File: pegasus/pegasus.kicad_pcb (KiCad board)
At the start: 2 copper layers, 50 x 120 mm, 17 parts, among them IC1 L7805ACV, IC2 RFD900, IC3 L70B-M39, J1 Screw_Terminal_01x02, U1 Teensy4.0, U2 CON-SMA-EDGE-S, U3 CON-SMA-EDGE-S

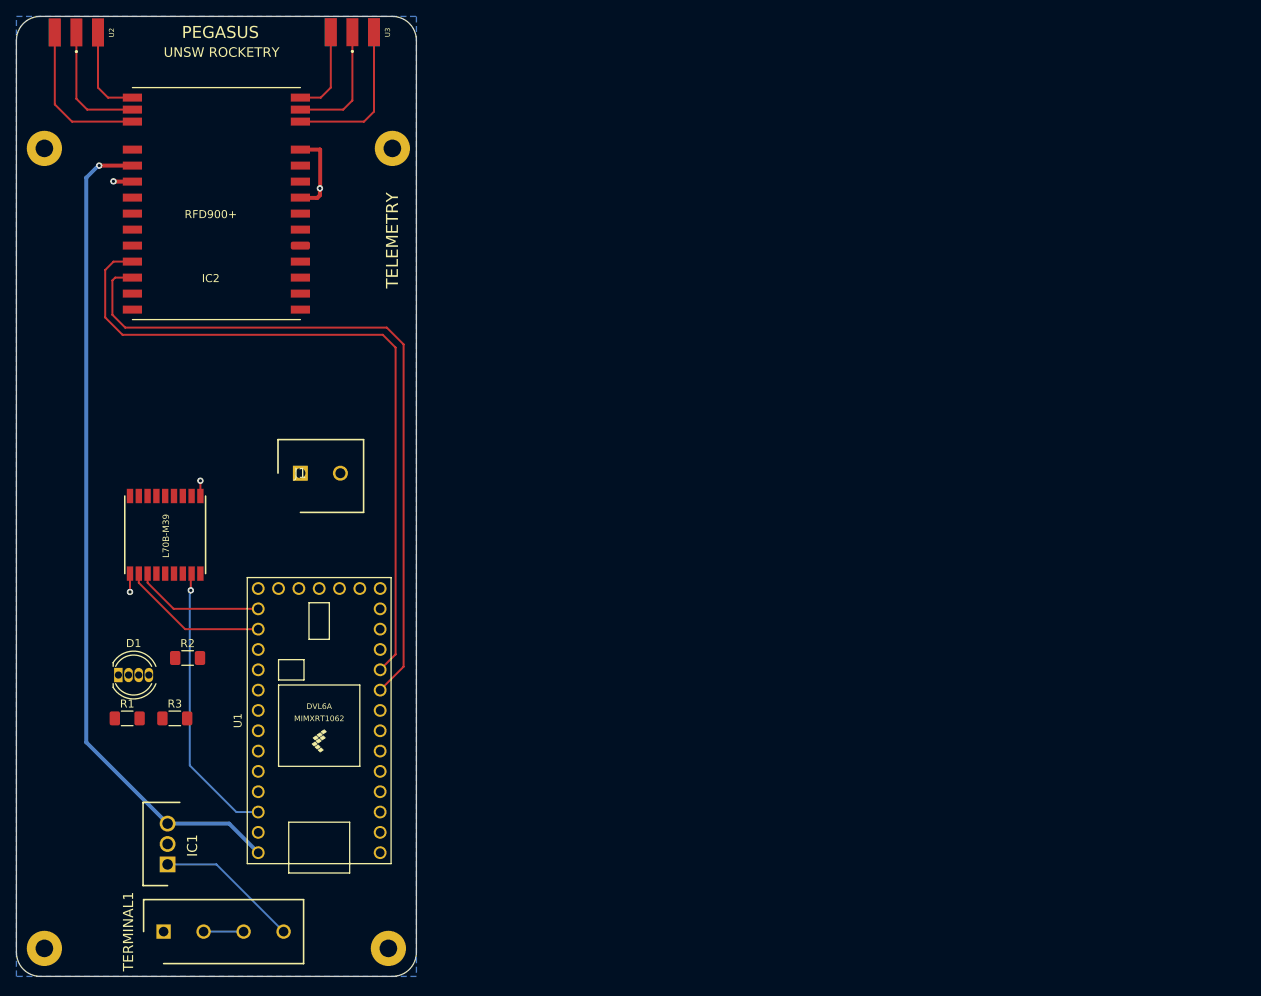
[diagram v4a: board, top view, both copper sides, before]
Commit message: change mount holes to m3, draft new component layout, reduce size  to 39x105mm
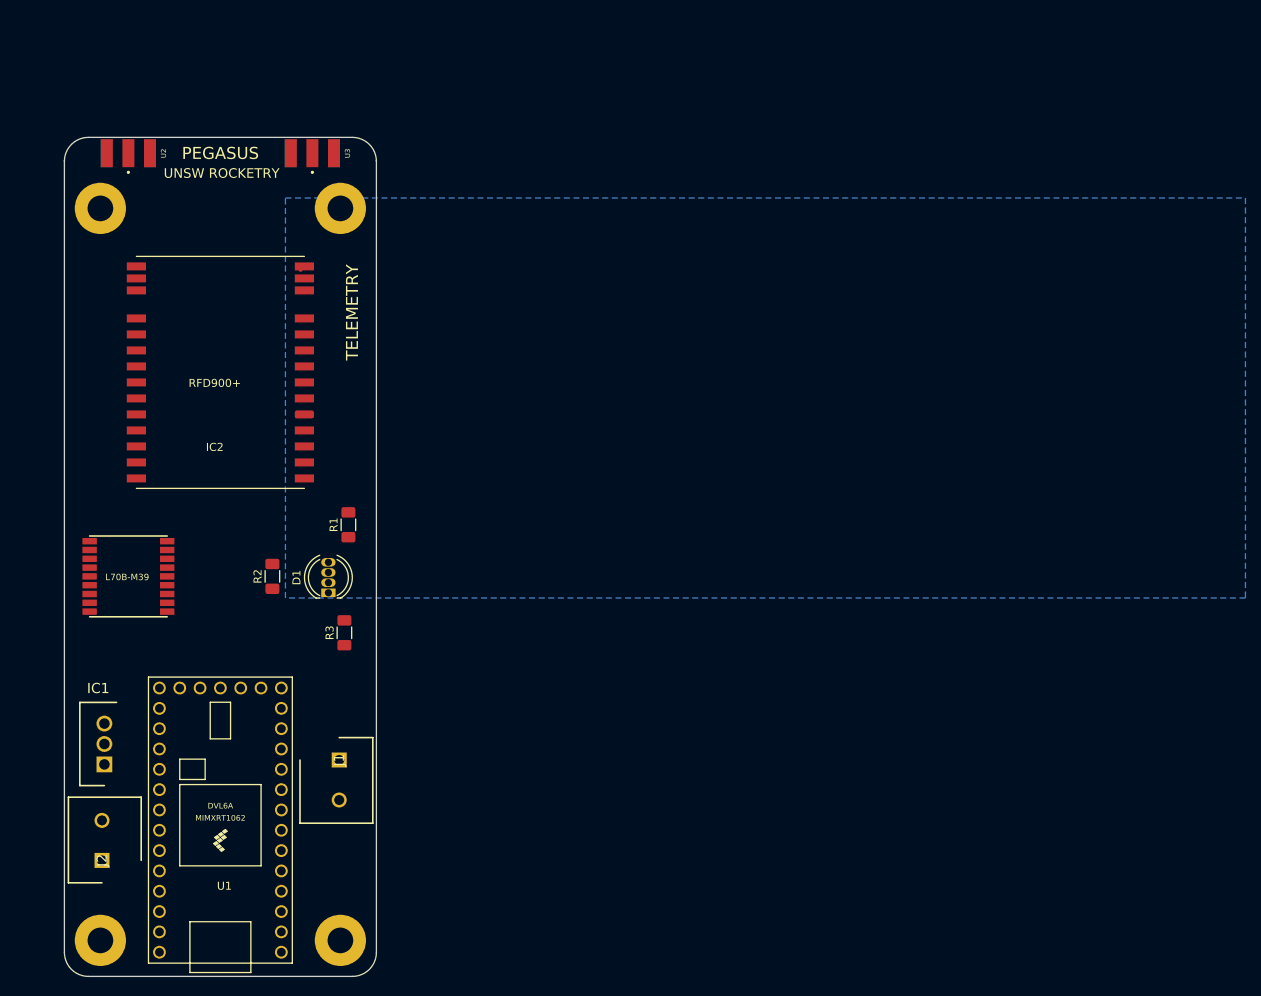
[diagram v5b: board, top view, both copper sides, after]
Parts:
- removed TERMINAL1: Screw_Terminal_01x04, RS-Components:SHDR4W100P0X500_1X4_2000X800X1000P
- added J2: Screw_Terminal_01x02, RS-Components:SHDR2W105P0X500_1X2_1060X900X1250P, F.Cu at (90.7, 145.5)
- H1, H2, H3, H4: footprint MountingHole:MountingHole_2.2mm_M2_Pad -> MountingHole:MountingHole_3.2mm_M3_Pad
- moved R1 36.7 mm to (121.5, 103.5), turned to 90 degrees
- moved J1 36.2 mm to (120.3, 132.9), turned to -90 degrees
- moved D1 28.2 mm to (119.0, 112.0), turned to 90 degrees
- moved G*** 26.5 mm to (105.0, 85.0)
- moved R3 23.7 mm to (121.0, 117.0), turned to 90 degrees
- moved IC2 21.1 mm to (110.0, 87.8)
- moved U1 17.5 mm to (105.5, 140.5)
- moved U2 16.4 mm to (94.0, 57.1)
- moved U3 15.9 mm to (117.0, 57.1)
- moved IC1 14.8 mm to (91.0, 133.5)
- moved R2 14.7 mm to (112.0, 110.0), turned to 90 degrees
- moved H4 10.3 mm to (90.5, 64.0)
- moved H3 9.92 mm to (120.5, 64.0)
- moved H1 7.07 mm to (90.5, 155.5)
- moved IC3 6.94 mm to (94.0, 110.0), turned to 0 degrees
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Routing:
- net +5V: track 104.1 -> 0.00 mm, vias 1 -> 0
- net RX7: track 89.3 -> 0.00 mm
- net TX7: track 88.7 -> 0.00 mm
- net 3.3V: track 35.0 -> 0.00 mm, vias 1 -> 0
- net Net-(IC2-Pad12): track 19.6 -> 0.00 mm
- net Net-(IC2-Pad17): track 19.6 -> 0.00 mm
- net RX3: track 18.5 -> 0.00 mm
- net /BATT+: track 18.0 -> 0.00 mm
- net GND: track 17.4 -> 0.00 mm, vias 4 -> 0
- net TX3: track 16.3 -> 0.00 mm
- net Net-(IC2-Pad16): track 15.9 -> 0.00 mm
- net Net-(IC2-Pad13): track 15.5 -> 0.00 mm
- net Net-(IC2-Pad15): track 11.7 -> 0.00 mm
- net Net-(IC2-Pad14): track 11.2 -> 0.06 mm
- net Net-(TERMINAL1-Pad2): track 5.00 -> 0.00 mm
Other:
- board size 50 x 120 mm -> 39 x 104.9 mm

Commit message: add second rx-tx screw terminal connector, optimize pin assignment for other components
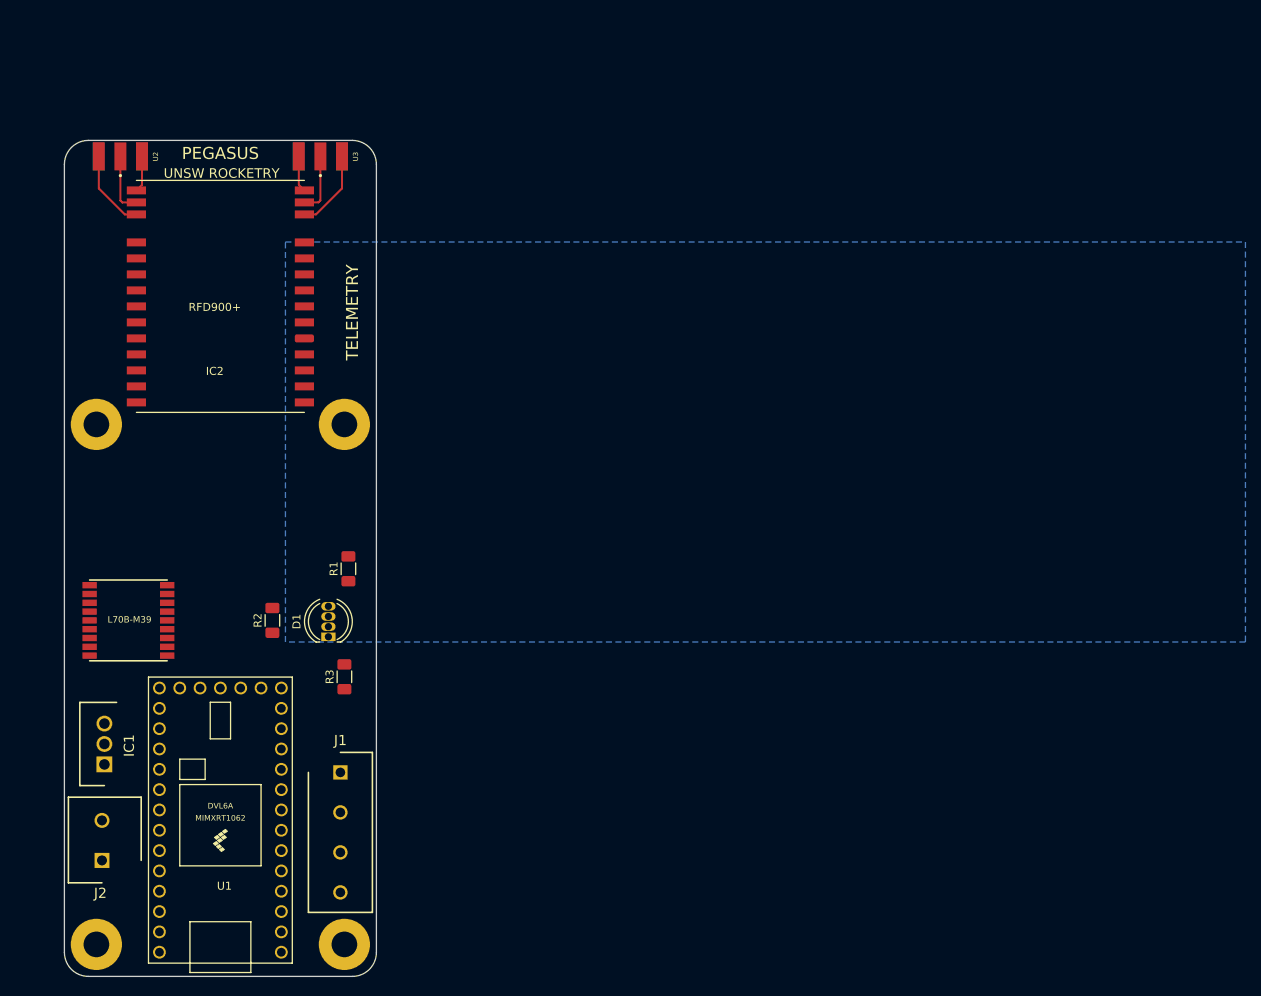
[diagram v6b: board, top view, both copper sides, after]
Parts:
- J1: value Screw_Terminal_01x02 -> Screw_Terminal_01x04; footprint RS-Components:SHDR2W105P0X500_1X2_1060X900X1250P -> RS-Components:SHDR4W100P0X500_1X4_2000X800X1000P
- moved H3 27.0 mm to (121.0, 91.0)
- moved H4 27.0 mm to (90.0, 91.0)
- moved IC2 9.50 mm to (110.0, 78.2)
- moved D1 5.50 mm to (119.0, 117.5)
- moved IC3 5.50 mm to (94.0, 115.5), turned to 180 degrees
- moved R1 5.50 mm to (121.5, 109.0)
- moved R2 5.50 mm to (112.0, 115.5)
- moved R3 5.50 mm to (121.0, 122.5)
- moved J1 1.56 mm to (120.5, 134.5)
- moved U2 1.08 mm to (93.0, 57.5)
- moved U3 1.08 mm to (118.0, 57.5)
- moved H1 0.71 mm to (90.0, 156.0)
- moved H2 0.71 mm to (121.0, 156.0)
- moved G*** 0.50 mm to (105.5, 85.0)
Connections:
- IC2 pad 25: TX7 -> TX3
- IC2 pad 26: RX7 -> RX3
- IC3 pad 2: RX3 -> RX4
- IC3 pad 3: TX3 -> TX4
- J1 pad 1: TX7 -> TX2
- J1 pad 2: RX7 -> RX2
- U1 pad 10: TX7 -> TX2
- U1 pad 2: unconnected-(U1-Pad2) -> RX1
- U1 pad 23: RGB1 -> RX4
- U1 pad 24: RGB2 -> TX4
- U1 pad 25: RGB3 -> unconnected-(U1-Pad25)
- U1 pad 3: unconnected-(U1-Pad3) -> TX1
- U1 pad 6: unconnected-(U1-Pad6) -> RGB1
- U1 pad 7: unconnected-(U1-Pad7) -> RGB2
- U1 pad 8: unconnected-(U1-Pad8) -> RGB3
- U1 pad 9: RX7 -> RX2
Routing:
- net Net-(IC2-Pad17): track 0.00 -> 10.5 mm
- net Net-(IC2-Pad12): track 0.00 -> 10.5 mm
- net Net-(IC2-Pad16): track 0.00 -> 8.01 mm
- net Net-(IC2-Pad13): track 0.00 -> 8.01 mm
- net Net-(IC2-Pad15): track 0.00 -> 4.95 mm
- net Net-(IC2-Pad14): track 0.06 -> 4.95 mm
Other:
- board size 39 x 104.9 mm -> 39 x 104.5 mm

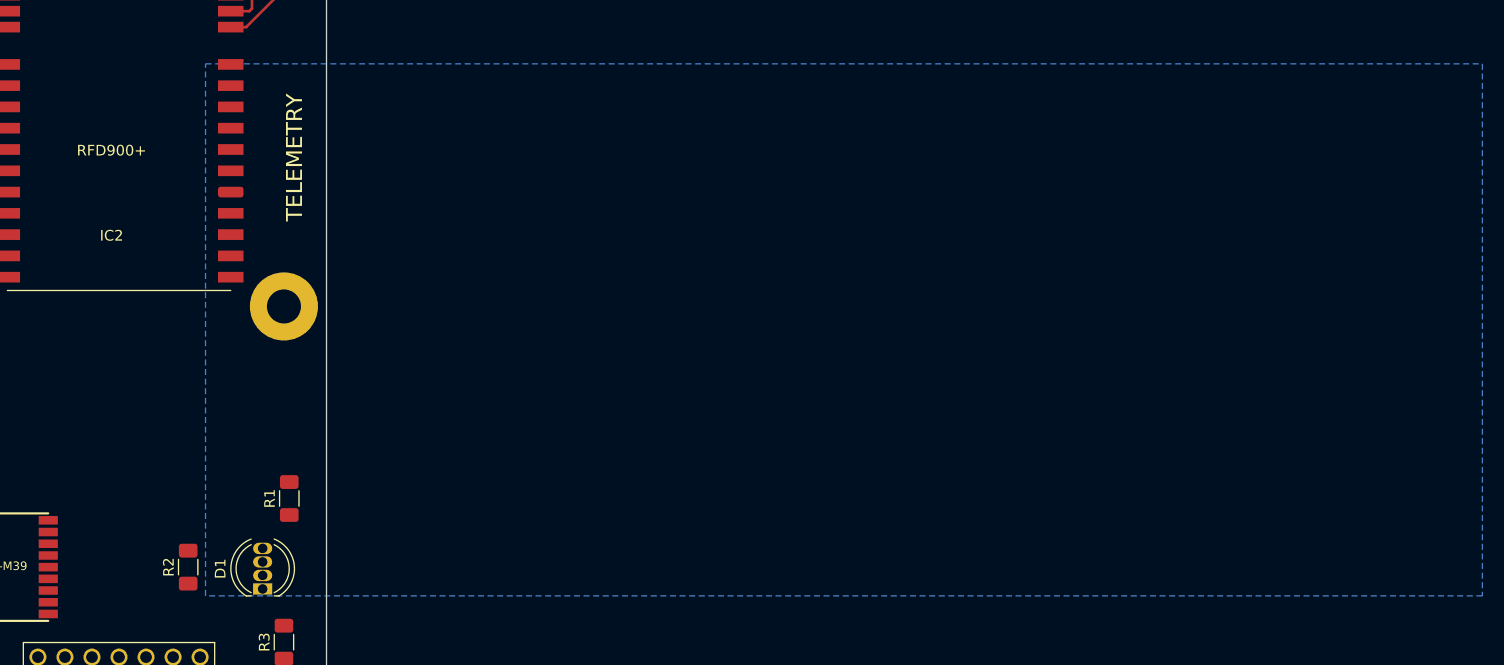
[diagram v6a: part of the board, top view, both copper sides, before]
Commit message: add xtsd footprint library, and xtsd nand chip to pcb
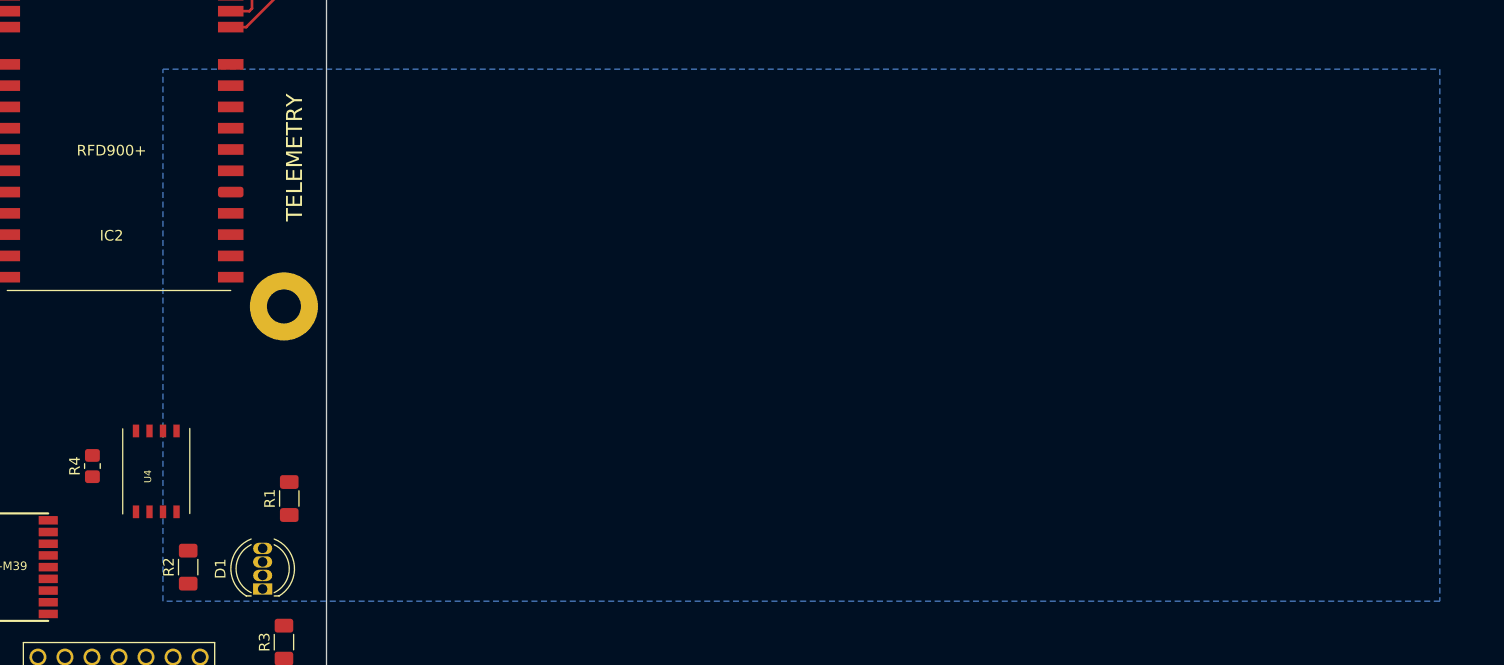
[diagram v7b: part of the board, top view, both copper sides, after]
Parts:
- added R4: 10k, Resistor_SMD:R_0805_2012Metric_Pad1.20x1.40mm_HandSolder, F.Cu at (103.0, 106.0)
- added U4: XTSD04GCLGEGA, XTSD:LGA8_8X6, F.Cu at (109.0, 106.5)
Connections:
- U1 pad 12: unconnected-(U1-Pad12) -> /CS
- U1 pad 13: unconnected-(U1-Pad13) -> /MOSI
- U1 pad 14: unconnected-(U1-Pad14) -> /MISO
- U1 pad 20: unconnected-(U1-Pad20) -> /SCK

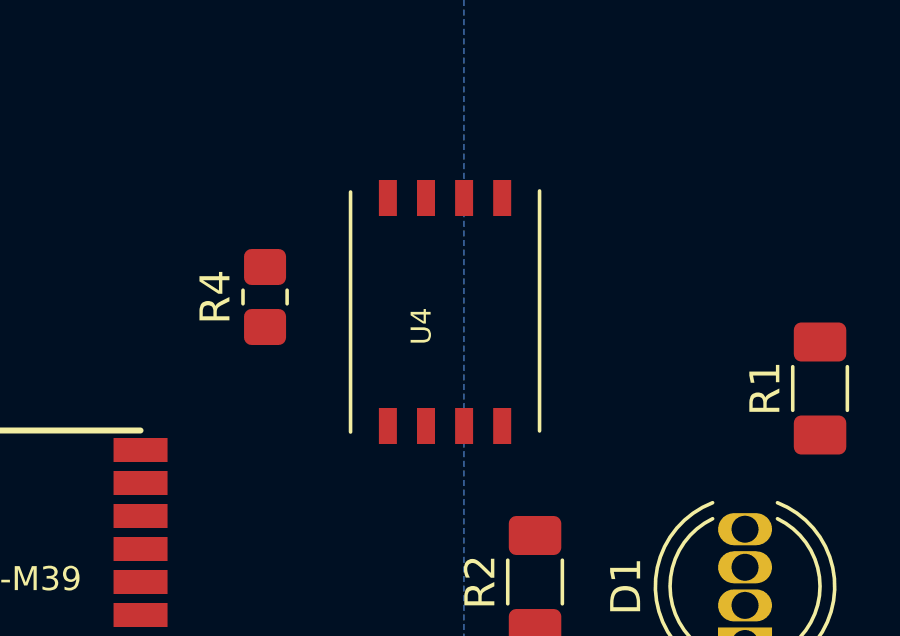
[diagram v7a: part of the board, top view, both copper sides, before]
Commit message: re add ground plane
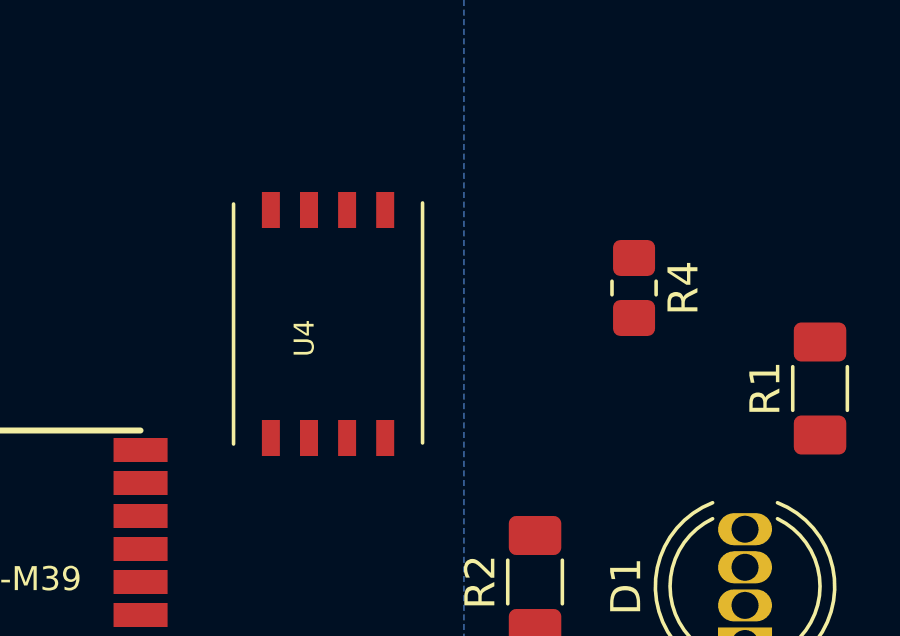
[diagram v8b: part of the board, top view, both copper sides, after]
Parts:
- moved R4 12.3 mm to (115.3, 105.7), turned to -90 degrees
- moved U4 3.92 mm to (105.1, 106.9)
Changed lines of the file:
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@@
   )
   (footprint "Resistor_SMD:R_0805_2012Metric_Pad1.20x1.40mm_HandSolder" (layer "F.Cu")
-    (at 103 106 90)
+    (at 115.3 105.7 -90)
     (descr "Resistor SMD 0805 (2012 Metric), square (rectangular) end terminal, IPC_7351 nominal with elongated pad for handsoldering. (Body size source: IPC-SM-782 page 72, https://www.pcb-3d.com/wordpress/wp-content/uploads/ipc-sm-782a_amendment_1_and_2.pdf), generated with kicad-footprint-generator")
     (tags "resistor handsolder")
@@
     (fp_line (start -1 0.625) (end -1 -0.625) (layer "F.Fab") (width 0.1))
     (fp_line (start 1 -0.625) (end 1 0.625) (layer "F.Fab") (width 0.1))
-    (pad "1" smd roundrect (at -1 0 90) (size 1.2 1.4) (layers "F.Cu" "F.Paste" "F.Mask") (roundrect_rratio 0.208333)
+    (pad "1" smd roundrect (at -1 0 270) (size 1.2 1.4) (layers "F.Cu" "F.Paste" "F.Mask") (roundrect_rratio 0.208333)
       (net 68 "+3.3V") (pintype "passive"))
-    (pad "2" smd roundrect (at 1 0 90) (size 1.2 1.4) (layers "F.Cu" "F.Paste" "F.Mask") (roundrect_rratio 0.208333)
+    (pad "2" smd roundrect (at 1 0 270) (size 1.2 1.4) (layers "F.Cu" "F.Paste" "F.Mask") (roundrect_rratio 0.208333)
       (net 69 "/CS") (pintype "passive"))
     (model "${KICAD6_3DMODEL_DIR}/Resistor_SMD.3dshapes/R_0805_2012Metric.wrl"
@@
   )
   (footprint "XTSD:LGA8_8X6" (layer "F.Cu")
-    (at 109 106.5 90)
+    (at 105.1 106.9 90)
     (descr "<b>Small Outline IC - 150mil Wide</b>")
     (property "LCSC" "C2759953")
